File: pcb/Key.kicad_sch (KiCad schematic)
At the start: 7 parts, among them U5 TMR2652D

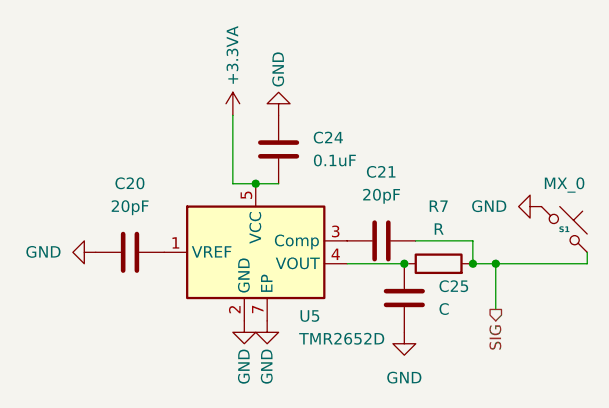
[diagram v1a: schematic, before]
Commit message: fix: moved D- and D+ to PB14 and PB15 for USB High Speed rather
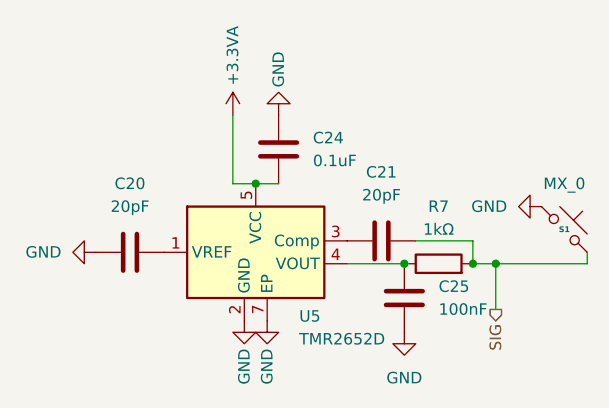
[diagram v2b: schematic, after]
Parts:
- C25: value C -> 100nF
- R7: value R -> 1kΩ
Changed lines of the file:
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@@
 			)
 		)
-		(property "Value" "C"
+		(property "Value" "100nF"
 			(at 106.68 69.8499 0)
 			(effects
@@
 			)
 		)
-		(property "Value" "R"
+		(property "Value" "1kΩ"
 			(at 106.68 60.96 90)
 			(effects

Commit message: feat: assigned footprints for each symbol and switch
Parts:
- removed C21: 20pF, symbol Device:C
- removed C25: 100nF, symbol Device:C
- removed S1: MX_0, symbol ScottoKeebs:Placeholder_Keyswitch
- C20: renamed from C24; footprint (none) -> Capacitor_SMD:C_0402_1005Metric
- C21: renamed from C20; footprint (none) -> Capacitor_SMD:C_0402_1005Metric
- R6: renamed from R7; footprint (none) -> Resistor_SMD:R_0402_1005Metric
- renumbered U5 to U4
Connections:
- net SIG renamed MX_IN
- no-connect marks 0 -> 1
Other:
- moved on the sheet: R6
